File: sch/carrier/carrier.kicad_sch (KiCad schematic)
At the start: 0 parts

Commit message: noice.
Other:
- added sheet connectors (connectors.kicad_sch)
- sheet CM4 ports: added +3.3v, BTN_A, BTN_B, DPAD_DOWN, DPAD_LEFT, DPAD_RIGHT, DPAD_UP; removed none
- sheet gamepad ports: added +3.3v, BTN_A, BTN_B, DPAD_DOWN, DPAD_LEFT, DPAD_RIGHT, DPAD_UP; removed none

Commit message: goodnight
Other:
- sheet PWR renamed PWR - BATT
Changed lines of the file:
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@@
     (stroke (width 0) (type solid) (color 0 0 0 0))
   )
-  (wire (pts (xy 101.6 38.1) (xy 120.65 38.1))
+  (wire (pts (xy 100.33 38.1) (xy 120.65 38.1))
     (stroke (width 0) (type solid) (color 0 0 0 0))
   )
-  (wire (pts (xy 101.6 40.64) (xy 120.65 40.64))
+  (wire (pts (xy 100.33 40.64) (xy 120.65 40.64))
     (stroke (width 0) (type solid) (color 0 0 0 0))
   )
-  (wire (pts (xy 101.6 43.815) (xy 120.65 43.815))
+  (wire (pts (xy 100.33 43.815) (xy 120.65 43.815))
     (stroke (width 0) (type solid) (color 0 0 0 0))
   )
-  (wire (pts (xy 101.6 46.355) (xy 120.65 46.355))
+  (wire (pts (xy 100.33 46.355) (xy 120.65 46.355))
     (stroke (width 0) (type solid) (color 0 0 0 0))
   )
-  (wire (pts (xy 101.6 50.165) (xy 120.65 50.165))
+  (wire (pts (xy 100.33 50.165) (xy 120.65 50.165))
     (stroke (width 0) (type solid) (color 0 0 0 0))
   )
-  (wire (pts (xy 101.6 52.705) (xy 120.65 52.705))
+  (wire (pts (xy 100.33 52.705) (xy 120.65 52.705))
     (stroke (width 0) (type solid) (color 0 0 0 0))
   )
@@
     )
   )
-  (sheet (at 213.995 115.57) (size 35.56 24.13) (fields_autoplaced)
+  (sheet (at 120.65 95.25) (size 44.45 23.495) (fields_autoplaced)
     (stroke (width 0.0006) (type solid) (color 0 0 0 0))
     (fill (color 0 0 0 0.0000))
-    (property "Sheet name" "PWR" (id 0) (at 213.995 114.9343 0)
+    (property "Sheet name" "PWR - BATT" (id 0) (at 120.65 94.6143 0)
       (effects (font (size 1.27 1.27)) (justify left bottom))
     )
-    (property "Sheet file" "power.kicad_sch" (id 1) (at 213.995 140.2087 0)
+    (property "Sheet file" "power.kicad_sch" (id 1) (at 120.65 119.2537 0)
       (effects (font (size 1.27 1.27)) (justify left top))
     )
   )
-  (sheet (at 120.65 101.6) (size 44.45 50.8) (fields_autoplaced)
+  (sheet (at 177.8 31.75) (size 44.45 50.8) (fields_autoplaced)
     (stroke (width 0.0006) (type solid) (color 0 0 0 0))
     (fill (color 0 0 0 0.0000))
-    (property "Sheet name" "connectors" (id 0) (at 120.65 100.9643 0)
+    (property "Sheet name" "connectors" (id 0) (at 177.8 31.1143 0)
       (effects (font (size 1.27 1.27)) (justify left bottom))
     )
-    (property "Sheet file" "connectors.kicad_sch" (id 1) (at 120.65 152.9087 0)
+    (property "Sheet file" "connectors.kicad_sch" (id 1) (at 177.8 83.0587 0)
       (effects (font (size 1.27 1.27)) (justify left top))
     )
   )
-  (sheet (at 65.405 31.75) (size 36.195 38.735) (fields_autoplaced)
+  (sheet (at 65.405 31.75) (size 34.925 50.8) (fields_autoplaced)
     (stroke (width 0.0006) (type solid) (color 0 0 0 0))
     (fill (color 0 0 0 0.0000))
@@
       (effects (font (size 1.27 1.27)) (justify left bottom))
     )
-    (property "Sheet file" "gamepad.kicad_sch" (id 1) (at 65.405 70.9937 0)
+    (property "Sheet file" "gamepad.kicad_sch" (id 1) (at 65.405 83.0587 0)
       (effects (font (size 1.27 1.27)) (justify left top))
     )
-    (pin "DPAD_UP" output (at 101.6 38.1 0)
+    (pin "DPAD_UP" output (at 100.33 38.1 0)
       (effects (font (size 1.27 1.27)) (justify right))
     )
-    (pin "DPAD_RIGHT" output (at 101.6 46.355 0)
+    (pin "DPAD_RIGHT" output (at 100.33 46.355 0)
       (effects (font (size 1.27 1.27)) (justify right))
     )
-    (pin "DPAD_DOWN" output (at 101.6 40.64 0)
+    (pin "DPAD_DOWN" output (at 100.33 40.64 0)
       (effects (font (size 1.27 1.27)) (justify right))
     )
-    (pin "DPAD_LEFT" output (at 101.6 43.815 0)
+    (pin "DPAD_LEFT" output (at 100.33 43.815 0)
       (effects (font (size 1.27 1.27)) (justify right))
     )
-    (pin "BTN_A" output (at 101.6 50.165 0)
+    (pin "BTN_A" output (at 100.33 50.165 0)
       (effects (font (size 1.27 1.27)) (justify right))
     )
-    (pin "BTN_B" output (at 101.6 52.705 0)
+    (pin "BTN_B" output (at 100.33 52.705 0)
       (effects (font (size 1.27 1.27)) (justify right))
     )

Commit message: hhhhhhhhhhhhhhhhh
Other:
- sheet gamepad renamed Buttons
- added sheet display board (display_board.kicad_sch)
- sheet CM4 ports: added +1.8v, +5v; removed none
- sheet PWR - BATT ports: added 5v; removed none

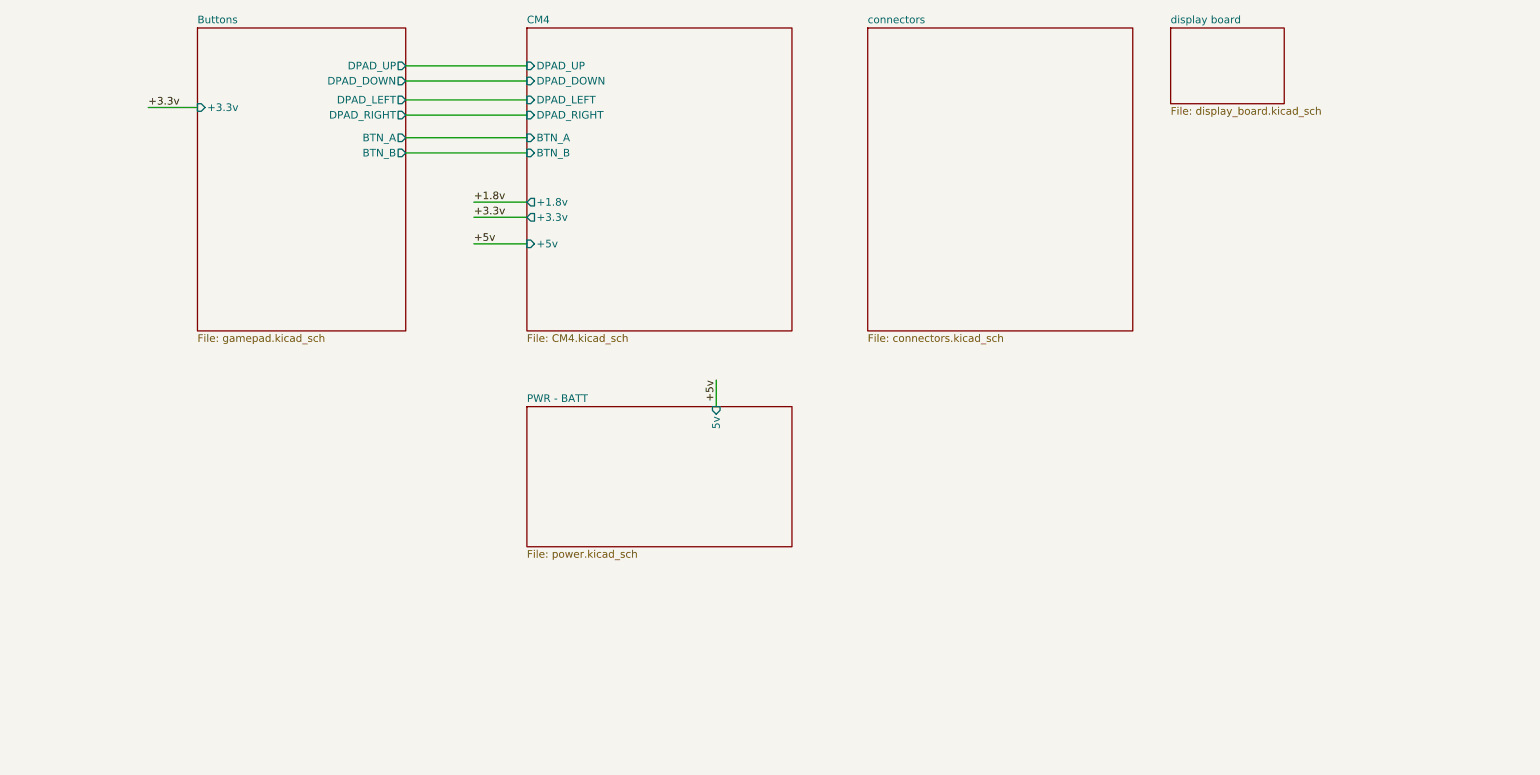
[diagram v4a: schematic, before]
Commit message: update readme and add some text for the sheets.
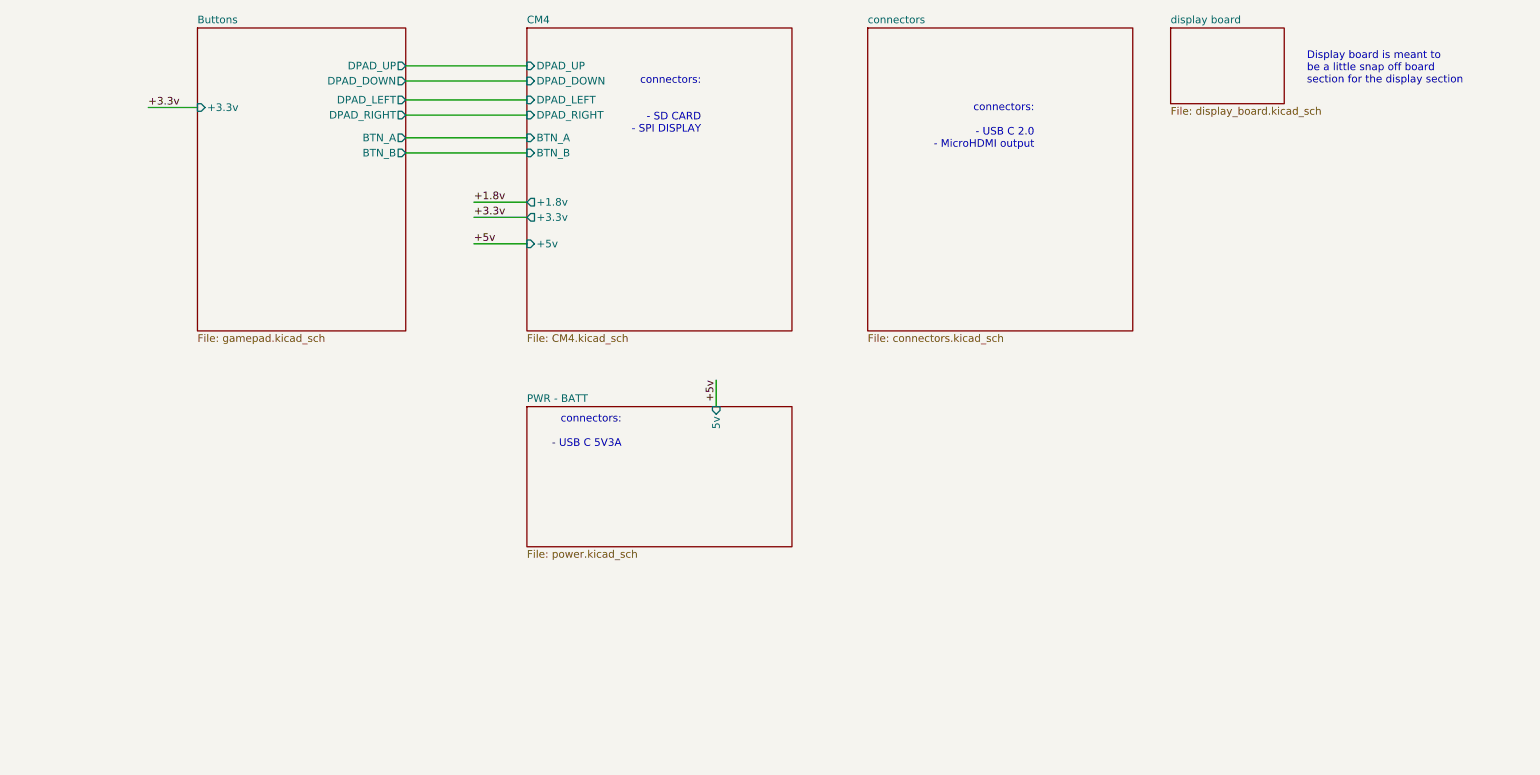
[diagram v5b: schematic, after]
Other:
- note added: "Display board is meant to be a little snap off board section for the display section"
- note added: "connectors: - SD CARD - SPI DISPLAY"
- note added: "connectors: - USB C 2.0 - MicroHDMI output"
- note added: "connectors: - USB C 5V3A"
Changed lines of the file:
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@@
     (stroke (width 0) (type solid) (color 0 0 0 0))
+  )
+  (text "connectors:\n\n- USB C 5V3A" (at 136.525 102.235 180)
+    (effects (font (size 1.27 1.27)) (justify right bottom))
+  )
+  (text "connectors:\n\n\n- SD CARD\n- SPI DISPLAY" (at 149.86 49.53 180)
+    (effects (font (size 1.27 1.27)) (justify right bottom))
+  )
+  (text "connectors:\n\n- USB C 2.0\n- MicroHDMI output" (at 205.74 52.07 180)
+    (effects (font (size 1.27 1.27)) (justify right bottom))
+  )
+  (text "Display board is meant to\nbe a little snap off board \nsection for the display section\n"
+    (at 251.46 41.275 0)
+    (effects (font (size 1.27 1.27)) (justify left bottom))
   )
   (label "+3.3v" (at 57.15 45.085 0)

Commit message: put some stuff on the pcb - it is going to kill me trying to get all on
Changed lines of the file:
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@@
       (effects (font (size 1.27 1.27)) (justify left top))
     )
-    (pin "5v" input (at 152.4 95.25 90)
+    (pin "5v" output (at 152.4 95.25 90)
       (effects (font (size 1.27 1.27)) (justify right))
     )
@@
       (reference "#PWR017") (unit 1) (value "GND") (footprint "")
     )
+    (path "/8d0ae364-2b30-4b7c-813a-81b59cbe3cd0/c4b55b50-ef94-4053-a500-7856df027f7e"
+      (reference "#PWR0101") (unit 1) (value "GND") (footprint "")
+    )
     (path "/59fee1d9-7f44-408e-bd4e-36f39b8a6086/21e52013-c61c-4fa9-a81e-68ab2f08a085"
       (reference "#PWR0102") (unit 1) (value "GND") (footprint "")
@@
     )
     (path "/8d0ae364-2b30-4b7c-813a-81b59cbe3cd0/f3edb616-9913-4597-bc50-c7867b516a30"
-      (reference "Q1") (unit 1) (value "BC557") (footprint "Package_TO_SOT_THT:TO-92_Inline")
+      (reference "Q1") (unit 1) (value "BC557") (footprint "Package_TO_SOT_THT:TO-92_Inline_Horizontal1")
     )
     (path "/8d0ae364-2b30-4b7c-813a-81b59cbe3cd0/a60f29ed-6aaf-4f6e-89b0-d3c088f4d967"
-      (reference "Q2") (unit 1) (value "BC557") (footprint "Package_TO_SOT_THT:TO-92_Inline")
+      (reference "Q2") (unit 1) (value "BC557") (footprint "Package_TO_SOT_THT:TO-92_Inline_Horizontal1")
     )
     (path "/59fee1d9-7f44-408e-bd4e-36f39b8a6086/d38f75a1-b8db-4168-9a94-afda41263ee2"
@@
       (reference "R18") (unit 1) (value "6.2k") (footprint "Resistor_SMD:R_0805_2012Metric_Pad1.20x1.40mm_HandSolder")
     )
+    (path "/95ef1699-d890-4da8-941a-b0ab341c2e25/34d10f0c-d7a0-40ac-b2ff-3f7f933d25b8"
+      (reference "R19") (unit 1) (value "33") (footprint "Resistor_SMD:R_0805_2012Metric_Pad1.20x1.40mm_HandSolder")
+    )
     (path "/59fee1d9-7f44-408e-bd4e-36f39b8a6086/56f68401-24a6-45fd-817b-cb90bd2ccdea"
       (reference "SW1") (unit 1) (value "SKRRACE010") (footprint "eec:ALPS-SKRRACE010-0-0-MFG")
@@
       (reference "TP2") (unit 1) (value "Activity") (footprint "TestPoint:TestPoint_Pad_2.0x2.0mm")
     )
+    (path "/59fee1d9-7f44-408e-bd4e-36f39b8a6086/fed6ec27-3f0f-4410-b670-7e022193596a"
+      (reference "TP6") (unit 1) (value "UP") (footprint "TestPoint:TestPoint_Pad_2.0x2.0mm")
+    )
+    (path "/59fee1d9-7f44-408e-bd4e-36f39b8a6086/bcf5c445-f538-446b-952a-580338cde548"
+      (reference "TP7") (unit 1) (value "DOWN") (footprint "TestPoint:TestPoint_Pad_2.0x2.0mm")
+    )
+    (path "/59fee1d9-7f44-408e-bd4e-36f39b8a6086/0f1969c3-9e42-42a5-b4ae-4bb8fbdbbbdb"
+      (reference "TP8") (unit 1) (value "LEFT") (footprint "TestPoint:TestPoint_Pad_2.0x2.0mm")
+    )
+    (path "/59fee1d9-7f44-408e-bd4e-36f39b8a6086/78e5283d-940c-4810-83f1-d3b6b4f50058"
+      (reference "TP9") (unit 1) (value "RIGHT") (footprint "TestPoint:TestPoint_Pad_2.0x2.0mm")
+    )
+    (path "/59fee1d9-7f44-408e-bd4e-36f39b8a6086/037e8592-f1ec-4554-8673-88100afd2616"
+      (reference "TP10") (unit 1) (value "A") (footprint "TestPoint:TestPoint_Pad_2.0x2.0mm")
+    )
+    (path "/59fee1d9-7f44-408e-bd4e-36f39b8a6086/57bd1f6a-9f88-4ef6-a2a5-b049bb1b3095"
+      (reference "TP11") (unit 1) (value "B") (footprint "TestPoint:TestPoint_Pad_2.0x2.0mm")
+    )
     (path "/59fee1d9-7f44-408e-bd4e-36f39b8a6086/e5ea8ed9-1334-45da-8719-957e7da56073"

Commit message: holy shit i hate chargers
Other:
- added sheet MC CTRL (stmcontrol.kicad_sch)
- note added: "connectors: - USB C 5V3A - I2C (Battery monitor)"
- note removed: "connectors: - USB C 5V3A"
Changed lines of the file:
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@@
     (stroke (width 0) (type solid) (color 0 0 0 0))
   )
-  (wire (pts (xy 152.4 90.805) (xy 152.4 95.25))
+  (wire (pts (xy 116.205 99.695) (xy 120.65 99.695))
     (stroke (width 0) (type solid) (color 0 0 0 0))
-  )
-  (text "connectors:\n\n- USB C 5V3A" (at 136.525 102.235 180)
-    (effects (font (size 1.27 1.27)) (justify right bottom))
   )
   (text "connectors:\n\n\n- SD CARD\n- SPI DISPLAY" (at 149.86 49.53 180)
     (effects (font (size 1.27 1.27)) (justify right bottom))
   )
+  (text "connectors:\n\n- USB C 5V3A\n- I2C (Battery monitor)\n"
+    (at 155.575 106.68 0)
+    (effects (font (size 1.27 1.27)) (justify right bottom))
+  )
   (text "connectors:\n\n- USB C 2.0\n- MicroHDMI output" (at 205.74 52.07 180)
     (effects (font (size 1.27 1.27)) (justify right bottom))
@@
     (effects (font (size 1.27 1.27)) (justify left bottom))
   )
-  (label "+5v" (at 152.4 90.805 270)
-    (effects (font (size 1.27 1.27)) (justify right bottom))
+  (label "+5v" (at 116.205 99.695 0)
+    (effects (font (size 1.27 1.27)) (justify left bottom))
   )
   (sheet (at 65.405 31.75) (size 34.925 50.8) (fields_autoplaced)
@@
     )
   )
-  (sheet (at 120.65 95.25) (size 44.45 23.495) (fields_autoplaced)
-    (stroke (width 0.0006) (type solid) (color 0 0 0 0))
-    (fill (color 0 0 0 0.0000))
-    (property "Sheet name" "PWR - BATT" (id 0) (at 120.65 94.6143 0)
-      (effects (font (size 1.27 1.27)) (justify left bottom))
-    )
-    (property "Sheet file" "power.kicad_sch" (id 1) (at 120.65 119.2537 0)
-      (effects (font (size 1.27 1.27)) (justify left top))
-    )
-    (pin "5v" output (at 152.4 95.25 90)
-      (effects (font (size 1.27 1.27)) (justify right))
+  (sheet (at 120.015 121.285) (size 21.59 24.13) (fields_autoplaced)
+    (stroke (width 0.0006) (type solid) (color 0 0 0 0))
+    (fill (color 0 0 0 0.0000))
+    (property "Sheet name" "MC CTRL" (id 0) (at 120.015 120.6493 0)
+      (effects (font (size 1.27 1.27)) (justify left bottom))
+    )
+    (property "Sheet file" "stmcontrol.kicad_sch" (id 1) (at 120.015 145.9237 0)
+      (effects (font (size 1.27 1.27)) (justify left top))
+    )
+  )
+  (sheet (at 120.65 92.71) (size 44.45 25.4) (fields_autoplaced)
+    (stroke (width 0.0006) (type solid) (color 0 0 0 0))
+    (fill (color 0 0 0 0.0000))
+    (property "Sheet name" "PWR - BATT" (id 0) (at 120.65 92.0743 0)
+      (effects (font (size 1.27 1.27)) (justify left bottom))
+    )
+    (property "Sheet file" "power.kicad_sch" (id 1) (at 120.65 118.6187 0)
+      (effects (font (size 1.27 1.27)) (justify left top))
+    )
+    (pin "5v" output (at 120.65 99.695 180)
+      (effects (font (size 1.27 1.27)) (justify left))
     )
   )
@@
     (path "/7d2c72bb-6811-42b4-a3fa-d7ba2c227aca" (page "5"))
     (path "/95ef1699-d890-4da8-941a-b0ab341c2e25" (page "6"))
+    (path "/37d166c5-a261-4942-8dd2-7ed8073b2036" (page "7"))
   )
   (symbol_instances
@@
       (reference "#PWR0103") (unit 1) (value "GND") (footprint "")
     )
+    (path "/8d0ae364-2b30-4b7c-813a-81b59cbe3cd0/15f8c83f-f558-4d91-b21e-dedfc95b0ef1"
+      (reference "#PWR?") (unit 1) (value "GND") (footprint "")
+    )
+    (path "/8d0ae364-2b30-4b7c-813a-81b59cbe3cd0/5bfba063-c27c-4ad2-a349-7596cda6ed94"
+      (reference "#PWR?") (unit 1) (value "GND") (footprint "")
+    )
+    (path "/8d0ae364-2b30-4b7c-813a-81b59cbe3cd0/a54628e7-a201-4869-8d21-5c051c131cb9"
+      (reference "#PWR?") (unit 1) (value "GND") (footprint "")
+    )
+    (path "/8d0ae364-2b30-4b7c-813a-81b59cbe3cd0/f746f4ac-5167-4c11-a4b6-cae66c382ef2"
+      (reference "#PWR?") (unit 1) (value "GND") (footprint "")
+    )
     (path "/59fee1d9-7f44-408e-bd4e-36f39b8a6086/c8a711c2-5c9c-43c5-8861-afaf43eb0347"
       (reference "C1") (unit 1) (value "0.1uF") (footprint "Capacitor_SMD:C_0504_1310Metric_Pad0.83x1.28mm_HandSolder")
@@
       (reference "C6") (unit 1) (value "0.1uF") (footprint "Capacitor_SMD:C_0504_1310Metric_Pad0.83x1.28mm_HandSolder")
     )
+    (path "/8d0ae364-2b30-4b7c-813a-81b59cbe3cd0/5712a26c-4e20-4598-9603-00bc21850deb"
+      (reference "C?") (unit 1) (value "4.7uF") (footprint "")
+    )
+    (path "/8d0ae364-2b30-4b7c-813a-81b59cbe3cd0/92ce5654-2617-48f1-ab71-3c0026809dcf"
+      (reference "C?") (unit 1) (value "10uF") (footprint "")
+    )
+    (path "/8d0ae364-2b30-4b7c-813a-81b59cbe3cd0/b5edea3c-fe64-45a3-aaef-f5c9c459ef4d"
+      (reference "C?") (unit 1) (value "4.7uF") (footprint "")
+    )
     (path "/19c5e008-dc4a-4080-a2ed-5cdad03792a4/86f057dd-5f37-4747-a676-a365d3666b91"
       (reference "D1") (unit 1) (value "LED") (footprint "LED_SMD:LED_0805_2012Metric_Pad1.15x1.40mm_HandSolder")
@@
       (reference "R19") (unit 1) (value "33") (footprint "Resistor_SMD:R_0805_2012Metric_Pad1.20x1.40mm_HandSolder")
     )
+    (path "/8d0ae364-2b30-4b7c-813a-81b59cbe3cd0/0de21fe4-a194-4d18-8007-d032bf68d967"
+      (reference "R?") (unit 1) (value "110k") (footprint "")
+    )
+    (path "/8d0ae364-2b30-4b7c-813a-81b59cbe3cd0/3f542c1c-13cd-438b-adcb-067253eda52c"
+      (reference "R?") (unit 1) (value "290k") (footprint "")
+    )
     (path "/59fee1d9-7f44-408e-bd4e-36f39b8a6086/56f68401-24a6-45fd-817b-cb90bd2ccdea"
       (reference "SW1") (unit 1) (value "SKRRACE010") (footprint "eec:ALPS-SKRRACE010-0-0-MFG")
@@
       (reference "U2") (unit 1) (value "ER-CON40HT-1") (footprint "ER-CON40HT-1:ER-CON40HT-1")
     )
-  )
+    (path "/8d0ae364-2b30-4b7c-813a-81b59cbe3cd0/57363998-be2d-4134-a962-796752eabb1f"
+      (reference "U?") (unit 1) (value "DS2745U") (footprint "Package_SO:TSSOP-8_3x3mm_P0.65mm")
+    )
+    (path "/8d0ae364-2b30-4b7c-813a-81b59cbe3cd0/72917145-318a-4003-abfb-3da619c5be0c"
+      (reference "U?") (unit 1) (value "MCP73871-2CC") (footprint "Package_DFN_QFN:QFN-20-1EP_4x4mm_P0.5mm_EP2.5x2.5mm")
+    )
+    (path "/8d0ae364-2b30-4b7c-813a-81b59cbe3cd0/a2dbcced-6947-4f3c-9ba0-a2d86c544a87"
+      (reference "U?") (unit 1) (value "MT3608") (footprint "Package_TO_SOT_SMD:SOT-23-6")
+    )
+    (path "/8d0ae364-2b30-4b7c-813a-81b59cbe3cd0/e67b34e9-4f9f-491f-a798-748ff91c7572"
+      (reference "U?") (unit 1) (value "TPS61230DRC") (footprint "Package_SON:Texas_S-PVSON-N10_ThermalVias")
+    )
+  )
